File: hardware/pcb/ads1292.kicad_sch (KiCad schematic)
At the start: 41 parts, among them J5 ECG pads, U8 ADS1292RIRSMT

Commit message: Fix the review's datasheet errors without changing respiration or the GDTs.
Replace the MCP73831 with a BQ25170 so a flat cell still charges from USB, add the missing series protection and ESP32/CP2102 passives, and withdraw the claim that respiration still works with 51 kΩ in the loop.

Co-authored-by: Riyu-D1 <Riyu-D1@users.noreply.github.com>
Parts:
- added C65: 1.5n, Capacitor_SMD:C_0402_1005Metric, symbol vitalq:C
- added C66: 1u, Capacitor_SMD:C_0402_1005Metric, symbol vitalq:C
- added R67, R68, R69: 10k, Resistor_SMD:R_0402_1005Metric, symbol vitalq:R
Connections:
- net GND: now also C66.2
- net IN1N: now also R68.2; no longer C51.2
- net IN1P: now also R67.2; no longer C50.2
- net RLDINV: now also C65.2
- net RLDOUT: now also C65.1, R69.2; no longer D3.1, R34.2
- net RLDREF: now also C66.1
- new net IN1N_AC: C51.2, R68.1
- new net IN1P_AC: C50.2, R67.1
- new net RLD_CLAMP: D3.1, R34.2, R69.1

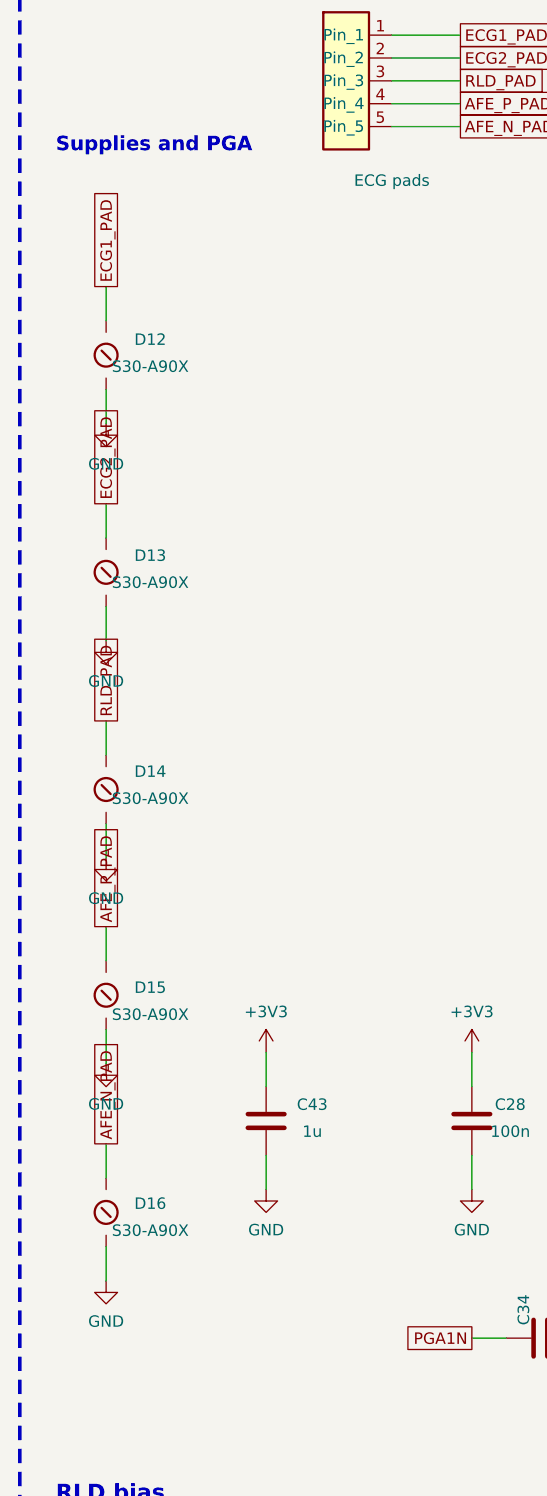
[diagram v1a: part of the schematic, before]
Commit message: Remove the gas-discharge tubes and pack the board to 36.5 by 45.6 mm.
D12-D20 and the S30 footprint are gone. Each patient line is now pad, 51 kΩ DPCR, TPD1E10B06, then the series resistor into the IC. A fourth creepage slot fills the gap the last tube was blocking.

Co-authored-by: Riyu-D1 <Riyu-D1@users.noreply.github.com>
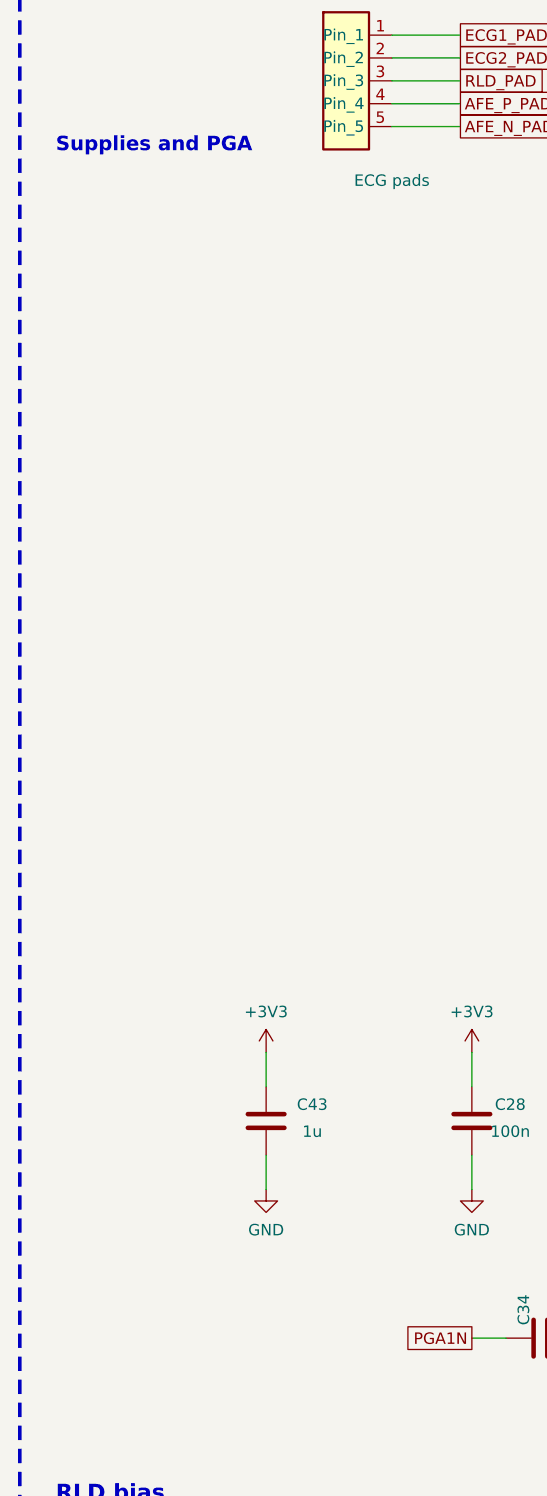
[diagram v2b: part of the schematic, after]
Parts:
- removed D12, D13, D14, D15, D16: S30-A90X, vitalq:GDT_S30, symbol vitalq:GDT

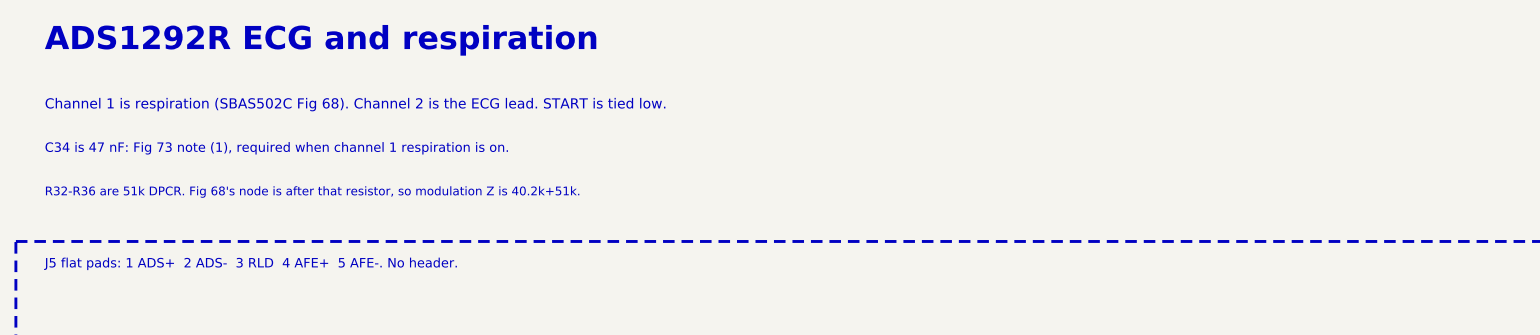
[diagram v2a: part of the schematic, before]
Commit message: Add a 4-wire chest respiration path on the AD5940.
The ADS1292R modulation network stays. Chest breathing uses four dedicated pads into AIN1, AIN0, AIN3, and AIN2, with the same pad-side surge chain and the datasheet isolation capacitors. Shoulder EDA remains on CE0, SE0, RE0, and DE0.

Co-authored-by: Riyu-D1 <Riyu-D1@users.noreply.github.com>
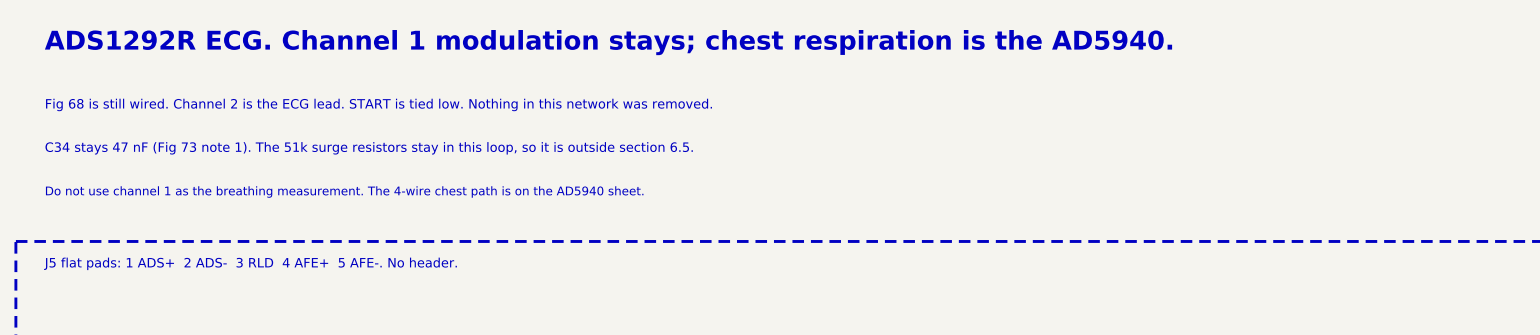
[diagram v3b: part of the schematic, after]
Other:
- note added: "ADS1292R ECG. Channel 1 modulation stays; chest respiration is the AD5940."
- note added: "C34 stays 47 nF (Fig 73 note 1). The 51k surge resistors stay in this loop, so it is outside section 6.5."
- note added: "Do not use channel 1 as the breathing measurement. The 4-wire chest path is on the AD5940 sheet."
- note added: "Fig 68 is still wired. Channel 2 is the ECG lead. START is tied low. Nothing in this network was removed."
- note removed: "ADS1292R ECG and respiration"
- note removed: "C34 is 47 nF: Fig 73 note (1), required when channel 1 respiration is on."
- note removed: "Channel 1 is respiration (SBAS502C Fig 68). Channel 2 is the ECG lead. START is tied low."
- note removed: "R32-R36 are 51k DPCR. Fig 68's node is after that resistor, so modulation Z is 40.2k+51k."

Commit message: Prepare hw_v1 for prefab review without claiming the route is finished.
Add the gauge TDFN, USB ESD, sense links, test access, and JLC BOM fields, and keep the partial Freerouting result with the remaining open nets listed.

Co-authored-by: Riyu-D1 <Riyu-D1@users.noreply.github.com>
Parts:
- added R100, R101: 10k, Resistor_SMD:R_0402_1005Metric, symbol vitalq:R
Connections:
- net GND: now also R100.2, R101.2
- net ADS_GPIO2: now reaches U8.25 (GPIO2/RCLK2)
- net ADS_GPIO2: now also R101.1
- net ADS_GPIO1: now reaches U8.26 (GPIO1/RCLK1)
- net ADS_GPIO1: now also R100.1
- net +3V3 renamed +3V3_ANA
- net SPI_MISO renamed MISO_ADS
- no-connect marks 3 -> 1
